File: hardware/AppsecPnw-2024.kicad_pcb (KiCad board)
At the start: 2 copper layers, 0 parts

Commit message: feat(Hw) Init PCB
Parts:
- added BZ1: Buzzer, Footprints:Buzzer4x4, F.Cu at (23.1, 42.6)
- added C10: .1uF, Capacitor_SMD:C_0603_1608Metric, F.Cu at (198.9, 85.9)
- added C11: .1uF, Capacitor_SMD:C_0603_1608Metric, F.Cu at (199.1, 91.9)
- added C12: .1uF, Capacitor_SMD:C_0603_1608Metric, F.Cu at (198.9, 89.8)
- added C13: .1uF, Capacitor_SMD:C_0603_1608Metric, F.Cu at (198.4, 87.8)
- added C14: .1uF, Capacitor_SMD:C_0603_1608Metric, B.Cu at (233.3, 57.1)
- added C15: .1uF, Capacitor_SMD:C_0603_1608Metric, B.Cu at (230.7, 80.2)
- added C3: 1uF, Capacitor_SMD:C_0603_1608Metric, B.Cu at (188.3, 34.5)
- added C4: 10uF, Capacitor_SMD:C_0603_1608Metric, B.Cu at (191.3, 34.5)
- added C5: 10uF, Capacitor_SMD:C_0603_1608Metric, B.Cu at (189.8, 34.5)
- added C7: 10uF, Capacitor_SMD:C_0603_1608Metric, B.Cu at (216.1, 34.1)
- added C9: 10uF, Capacitor_SMD:C_0603_1608Metric, B.Cu at (208.3, 34.5)
- added D1: MBR120, Diode_SMD:D_SOD-123F, B.Cu at (211.6, 40.5)
- added D2: MBR120, Diode_SMD:D_SOD-123F, F.Cu at (27.4, 37.1)
- added D3: LED, LED_SMD:LED_0805_2012Metric_Pad1.15x1.40mm_HandSolder, F.Cu at (128.2, 36.2)
- added D4: LED, LED_SMD:LED_0805_2012Metric_Pad1.15x1.40mm_HandSolder, F.Cu at (128.2, 39.2)
- added F1: 0.5A, Fuse:Fuse_0805_2012Metric, B.Cu at (232.2, 42.0)
- added G***: LOGO, Aesthetics:electronic_cats_logo_8x6, B.Cu at (188.3, 81.6)
- added G***: LOGO, LOGO, B.Cu at (225.0, 82.5)
- added J1: OLED, Connector_PinHeader_2.54mm:PinHeader_1x04_P2.54mm_Vertical, F.Cu at (186.2, 60.8)
- added J2: Battery, Footprints:BAT-TH_BH-AAA-A1AJ024, B.Cu at (180.8, 59.3)
- added J3: I2C, Connector_PinHeader_2.54mm:PinHeader_1x04_P2.54mm_Vertical, F.Cu at (132.0, 53.1)
- added J4: UART, Connector_PinHeader_2.54mm:PinHeader_1x05_P2.54mm_Vertical, F.Cu at (127.3, 65.4)
- added P1: USB_C_Plug_USB2.0, Footprints:C393939, B.Cu at (232.1, 49.0)
- added Q1: DMG3415U-7, Package_TO_SOT_SMD:SOT-23, B.Cu at (208.3, 40.3)
- added Q2: MMBT2222A, Package_TO_SOT_SMD:SOT-23, F.Cu at (20.2, 34.6)
- added R1: 100K, Resistor_SMD:R_0603_1608Metric, B.Cu at (212.4, 37.3)
- added R2: 1K, Resistor_SMD:R_0603_1608Metric, F.Cu at (19.9, 38.1)
- added R4: 1K, Resistor_SMD:R_0603_1608Metric, F.Cu at (135.0, 37.0)
- added R5: 1K, Resistor_SMD:R_0603_1608Metric, F.Cu at (135.0, 39.5)
- added R6: 5k1, Resistor_SMD:R_0603_1608Metric, B.Cu at (228.7, 46.9)
- added R7: 5k1, Resistor_SMD:R_0603_1608Metric, B.Cu at (228.7, 51.5)
- added R8: 10K, Resistor_SMD:R_0603_1608Metric, B.Cu at (227.6, 63.4)
- added Ref**: Val**, Badge pnwcon, F.Cu at (198.7, 67.3)
- added SW1: ON, Footprints:JS102011SAQN, B.Cu at (234.3, 35.5)
- added SW2: LEFT, Button_Switch_SMD:SW_SPST_TL3342, F.Cu at (185.0, 87.2)
- added SW3: DOWN, Button_Switch_SMD:SW_SPST_TL3342, F.Cu at (201.4, 100.7)
- added SW4: UP, Button_Switch_SMD:SW_SPST_TL3342, F.Cu at (201.4, 75.8)
- added SW5: RIGTH, Button_Switch_SMD:SW_SPST_TL3342, F.Cu at (215.4, 87.1)
- added SW6: RESET, Button_Switch_SMD:SW_SPST_TL3342, B.Cu at (233.3, 63.4)
- added SW7: GPIO, Button_Switch_SMD:SW_SPST_TL3342, B.Cu at (230.7, 73.4)
- added U1: ESP32-C6-WROOM-1U-N4, Footprints:MOD28_ESP32-C6-WROOM-1U_EXP, B.Cu at (175.8, 42.3)
- added U4: AP2112K-3.3, Package_TO_SOT_SMD:SOT-23-5, B.Cu at (212.3, 34.5)
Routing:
- added copper zone on B.Cu, net GND
- added copper zone on F.Cu, net GND
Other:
- board outline added: 75.2 x 76.5 mm
- net class Default removed
- board text added: "31337 H4x0r"
- board text added: "pwnCON Badge"
- board text added: "v1.0"

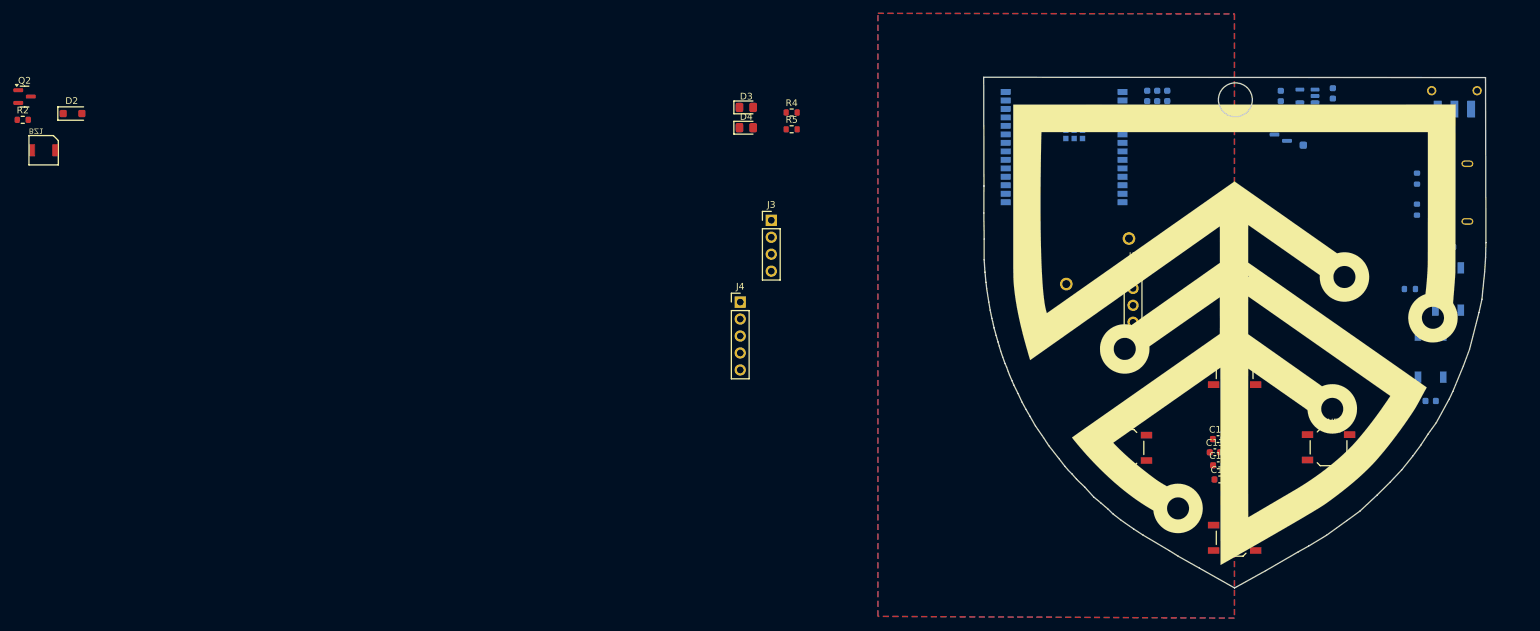
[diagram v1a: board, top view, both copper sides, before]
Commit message: feat(Hw) Update schematic and floorplan
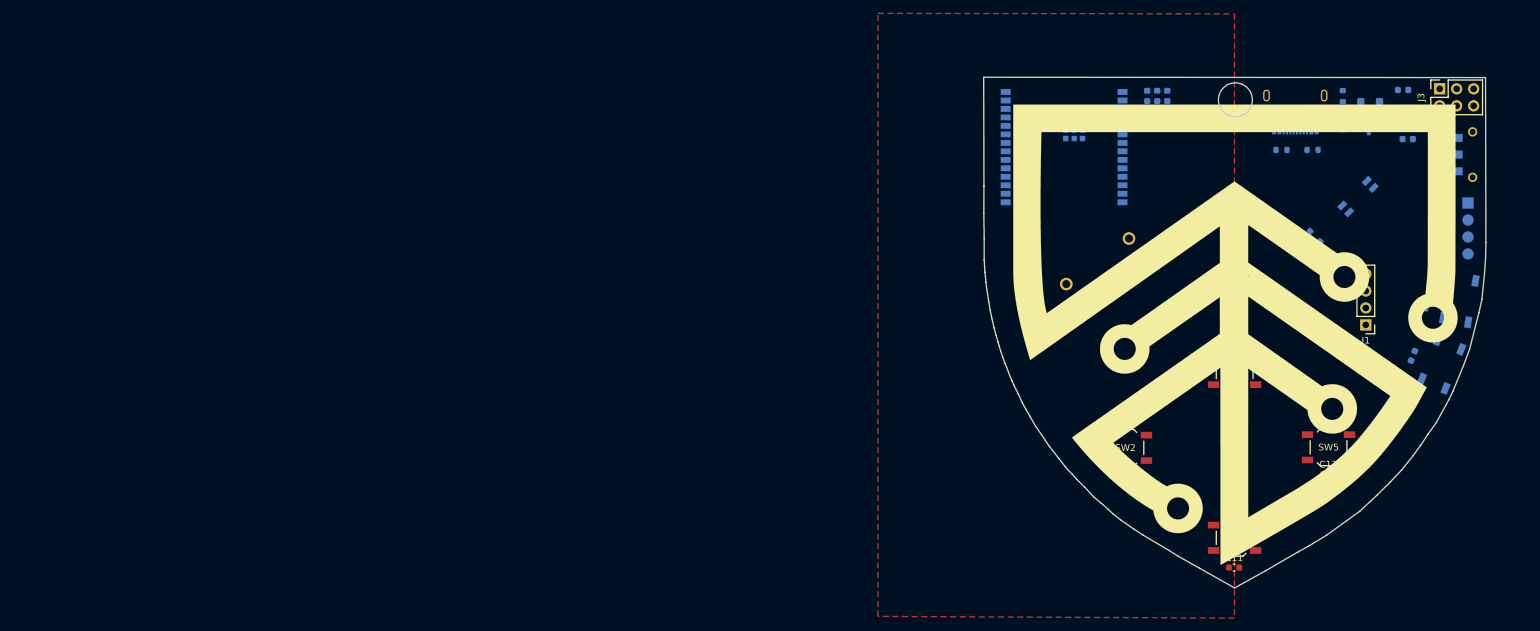
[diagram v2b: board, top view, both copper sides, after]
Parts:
- removed BZ1: Buzzer, Footprints:Buzzer4x4
- removed D3, D4: LED, LED_SMD:LED_0805_2012Metric_Pad1.15x1.40mm_HandSolder
- removed J4: UART, Connector_PinHeader_2.54mm:PinHeader_1x05_P2.54mm_Vertical
- removed Q2: MMBT2222A, Package_TO_SOT_SMD:SOT-23
- removed R5: 1K, Resistor_SMD:R_0603_1608Metric
- added J5: UART, Footprints:PinHeader_1x04_P2.54mm_Vertical, B.Cu at (236.3, 50.5)
- added R3: 330, Resistor_SMD:R_0603_1608Metric, B.Cu at (213.6, 56.9)
- D2: value MBR120 -> LED_RABG; footprint Diode_SMD:D_SOD-123F -> Footprints:AAA3528SURKCGKC09; moved to B.Cu
- J1: footprint Connector_PinHeader_2.54mm:PinHeader_1x04_P2.54mm_Vertical -> Footprints:Display OLED 128 x32
- J3: value I2C -> Conn_02x03_Odd_Even; footprint Connector_PinHeader_2.54mm:PinHeader_1x04_P2.54mm_Vertical -> Connector_PinSocket_2.54mm:PinSocket_2x03_P2.54mm_Vertical
- R2, R4: value 1K -> 330; moved to B.Cu
- moved R2 193.0 mm to (212.1, 55.3), turned to 45 degrees
- moved D2 192.8 mm to (219.8, 49.6), turned to -135 degrees
- moved J3 102.0 mm to (232.1, 33.4), turned to 90 degrees
- moved R4 83.7 mm to (215.8, 58.9), turned to 45 degrees
- moved J1 35.8 mm to (221.0, 68.8), turned to 180 degrees
- moved P1 24.0 mm to (210.4, 38.6), turned to 0 degrees
- moved R6 20.7 mm to (208.4, 42.6), turned to 0 degrees
- moved C9 20.1 mm to (227.3, 41.0), turned to 0 degrees
- moved R7 18.0 mm to (213.0, 42.6), turned to 180 degrees
- moved C13 17.3 mm to (215.4, 91.1)
- moved U4 15.4 mm to (227.3, 37.6), turned to -90 degrees
- moved F1 15.0 mm to (217.6, 38.5), turned to 90 degrees
- moved C10 14.7 mm to (185.3, 91.5)
- moved C11 13.4 mm to (201.3, 105.1)
- moved Q1 13.3 mm to (221.4, 38.7), turned to -90 degrees
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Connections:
- D2 pad 1: +3V3 -> Net-(D2-RK)
- D2 pad 2: Net-(BZ1-+) -> +3V3
- J3 pad 2: /SCL -> GND
- J3 pad 4: GND -> /SCL
- R2 pad 1: /Buzz -> /RED
- R2 pad 2: Net-(Q2-B) -> Net-(D2-RK)
- R4 pad 1: Net-(D3-K) -> /BLUE
- R4 pad 2: GND -> Net-(D2-BK)
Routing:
- removed copper zone on B.Cu, net GND

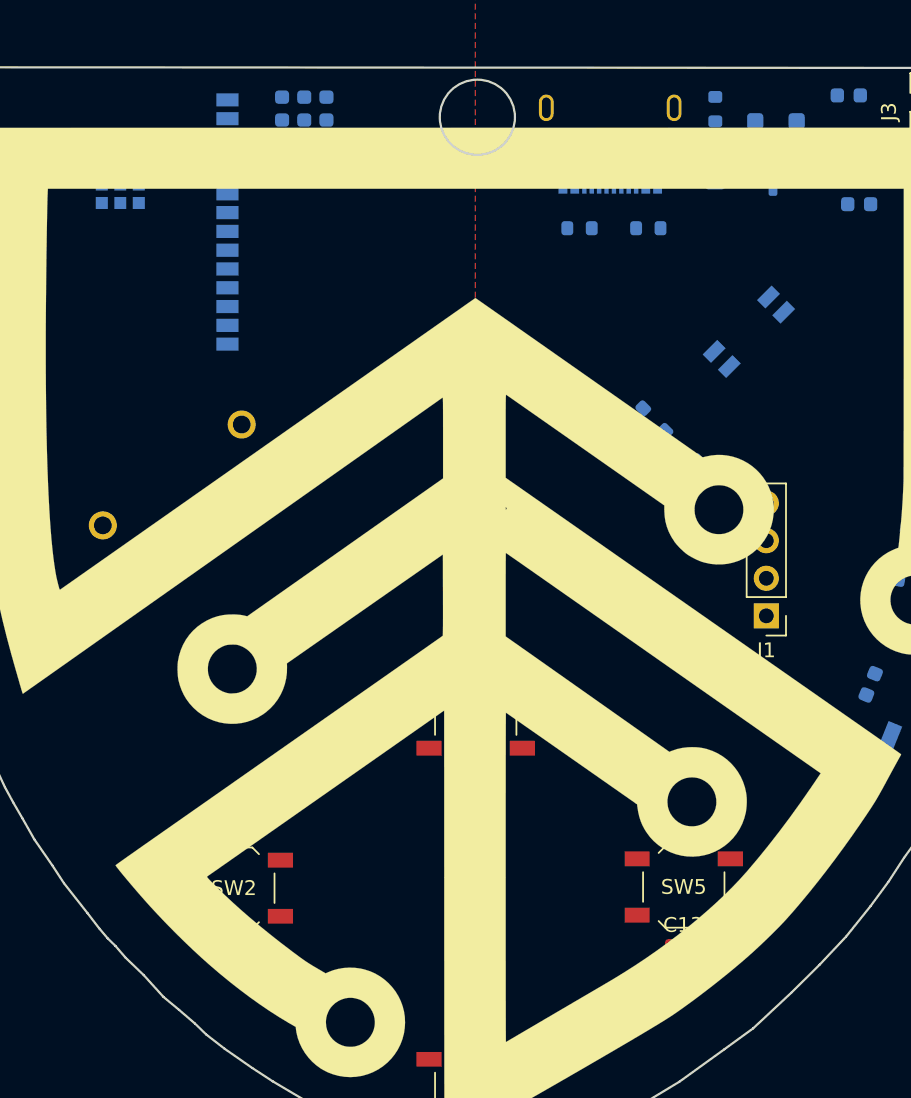
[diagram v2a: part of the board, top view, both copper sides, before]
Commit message: feat(Hw) Update schematic
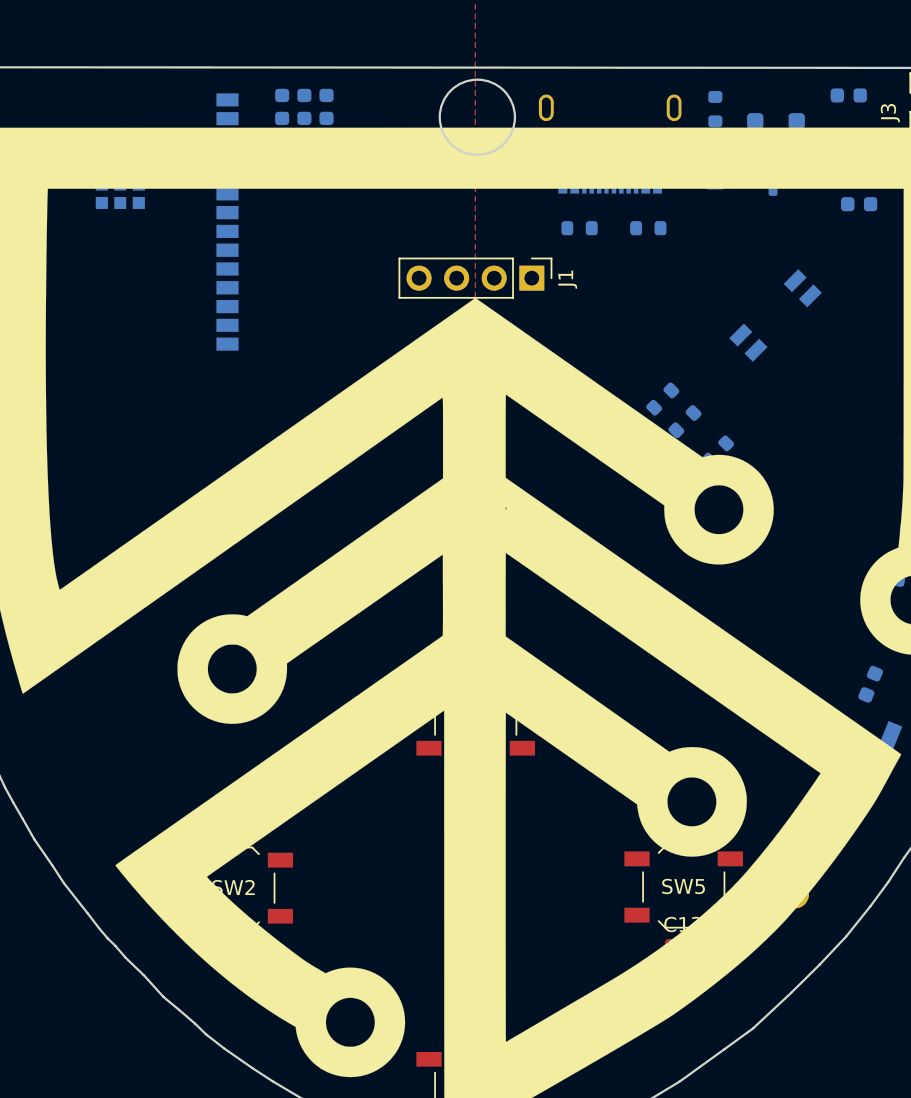
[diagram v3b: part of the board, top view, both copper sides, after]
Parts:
- moved J2 49.1 mm to (218.2, 91.0), turned to -54 degrees
- moved J1 27.8 mm to (205.2, 46.0), turned to -90 degrees
- moved R2 2.25 mm to (214.0, 54.1)
- moved R3 2.25 mm to (215.5, 55.6)
- moved R4 2.25 mm to (217.7, 57.7)
- moved D2 2.11 mm to (221.6, 48.5)
- moved C3 0.12 mm to (188.3, 34.4)
- moved C4 0.12 mm to (191.3, 34.4)
- moved C5 0.12 mm to (189.8, 34.4)
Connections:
- U1 pad 11: /DIO11 -> unconnected-(U1-IO10-Pad11)
- U1 pad 12: /LED2 -> /BLUE
- U1 pad 16: /CS -> unconnected-(U1-IO18-Pad16)
- U1 pad 17: /COPI -> unconnected-(U1-IO19-Pad17)
- U1 pad 18: /CIPO -> unconnected-(U1-IO20-Pad18)
- U1 pad 19: /SCK -> unconnected-(U1-IO21-Pad19)
- U1 pad 26: /LED1 -> /GREEN
- U1 pad 27: /Buzz -> /RED
- U1 pad 4: /RX1 -> unconnected-(U1-IO4-Pad4)
- U1 pad 5: /TX1 -> unconnected-(U1-IO5-Pad5)
- U1 pad 8: /CD -> unconnected-(U1-IO40-Pad8)

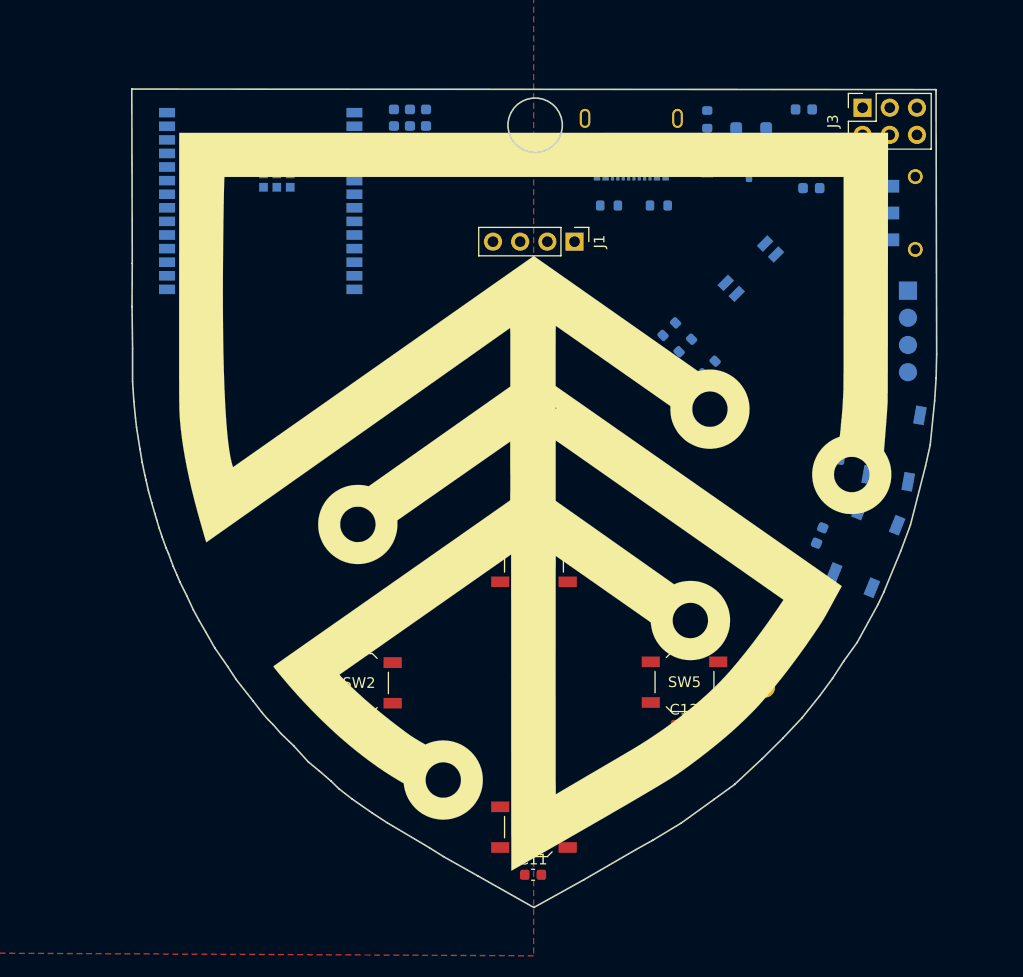
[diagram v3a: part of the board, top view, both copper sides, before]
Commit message: feat(Hw): Update schematic and init route
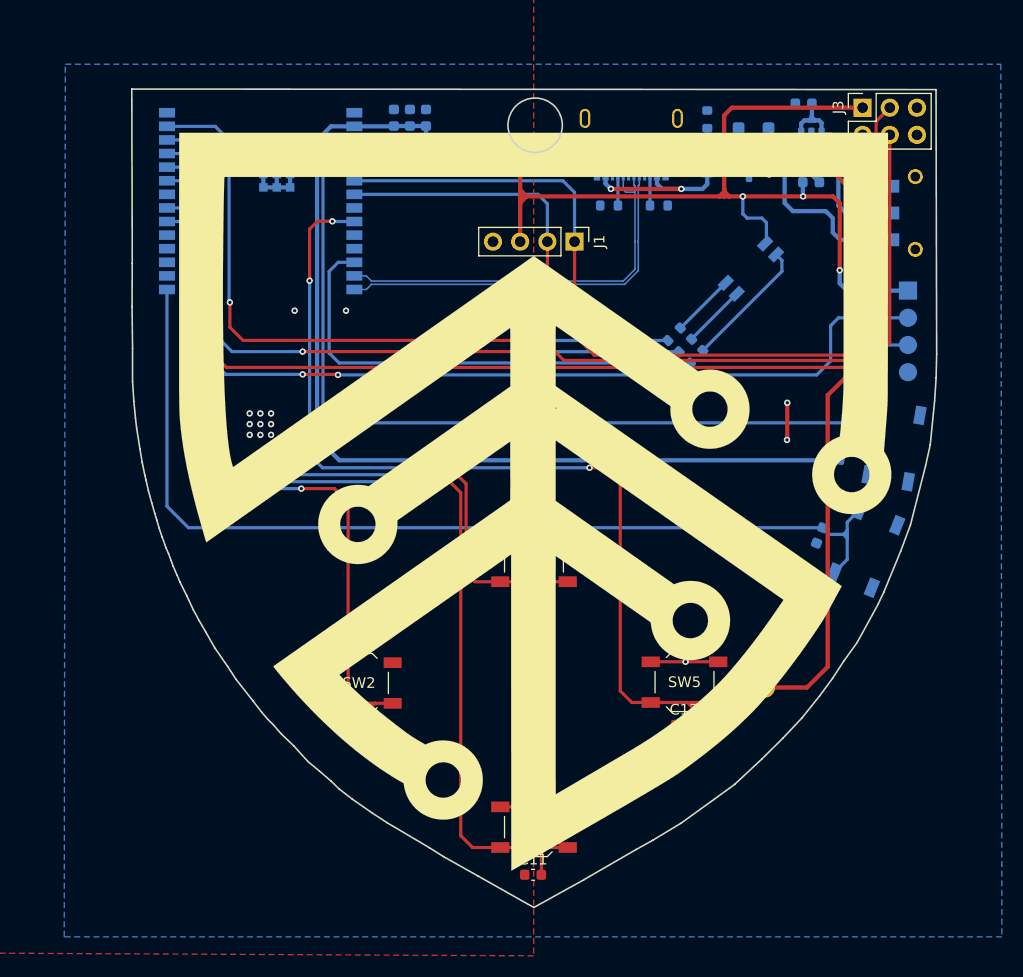
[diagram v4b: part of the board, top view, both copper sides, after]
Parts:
- removed U1: ESP32-C6-WROOM-1U-N4, Footprints:MOD28_ESP32-C6-WROOM-1U_EXP
- added U2: ESP32-C6-WROOM-1-N4, Footprints:ESP32C6WROOM1N4, B.Cu at (175.8, 39.2)
- added kibuzzard-660EEC06: G***, kibuzzard-660EEC06, B.Cu at (232.8, 50.5)
- added kibuzzard-660EEC1C: G***, kibuzzard-660EEC1C, B.Cu at (233.4, 53.1)
- added kibuzzard-660EEC32: G***, kibuzzard-660EEC32, B.Cu at (233.4, 55.6)
- added kibuzzard-660EEC49: G***, kibuzzard-660EEC49, B.Cu at (233.2, 58.1)
- added kibuzzard-660EECB7: G***, kibuzzard-660EECB7, B.Cu at (229.8, 33.4)
- added kibuzzard-660EEDFA: G***, kibuzzard-660EEDFA, B.Cu at (229.8, 36.0)
- SW7: value GPIO -> BOOT
- moved R4 1.52 mm to (216.6, 56.7)
- moved R2 0.65 mm to (214.4, 54.6)
- moved C9 0.55 mm to (227.2, 40.4)
- moved U4 0.55 mm to (227.3, 37.1)
- moved C7 0.55 mm to (226.6, 33.0)
- moved D1 0.22 mm to (221.9, 35.3)
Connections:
- J5 pad 1: +3.3V -> +3V3
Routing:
- net +3V3: track 0.00 -> 184.9 mm, vias 0 -> 4
- net /DOWN: track 0.00 -> 98.5 mm, vias 0 -> 1
- net /BOOT: track 0.00 -> 92.8 mm
- net /RX: track 0.00 -> 91.6 mm, vias 0 -> 2
- net /EN: track 0.00 -> 90.1 mm
- net /TX: track 0.00 -> 89.7 mm, vias 0 -> 2
- net /SELECT: track 0.00 -> 88.5 mm, vias 0 -> 3
- net /SDA: track 0.00 -> 86.2 mm
- net /SCL: track 0.00 -> 84.2 mm
- net /UP: track 0.00 -> 75.8 mm, vias 0 -> 1
- net /BACK: track 0.00 -> 71.1 mm, vias 0 -> 1
- net /GREEN: track 0.00 -> 66.5 mm, vias 0 -> 2
- net /RED: track 0.00 -> 65.3 mm, vias 0 -> 2
- net +BATT: track 0.00 -> 62.0 mm, vias 0 -> 3
- net GND: track 0.00 -> 52.3 mm, vias 0 -> 15
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- added copper zone on B.Cu, net GND

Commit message: feat(hw):add logos
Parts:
- moved G*** 38.2 mm to (221.6, 62.8)
- moved G*** 36.4 mm to (210.5, 49.0)
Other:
- board text added: "AppSecpnwCON Badge"
- board text added: "My TEAM is:"
- board text added: "RED TEAM Vs BLUE TEAM"
- board text added: "choose your team"
- board text added: "v2.0"
- board text removed: "31337 H4x0r"
- board text removed: "pwnCON Badge"
- board text removed: "v1.0"
